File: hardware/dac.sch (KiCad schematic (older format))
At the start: 1 part

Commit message: Update schematics
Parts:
- added J?: JACK_V_OCT, symbol thonkiconn_jackSocket_fuzzySi:fuzzySI_thonkiconn
- added R?: 7.7k, symbol Device:R
- added R?: 10k, symbol Device:R
- added U? (x2): LM324, symbol Amplifier_Operational:LM324
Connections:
- net labels added: +12V
- wire segments 6 -> 18
- no-connect marks 1 -> 2
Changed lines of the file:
@@
 $EndComp
 Wire Wire Line
-	5600 3700 5600 4000
+	5600 3700 5600 3900
 $Comp
 L power:GND #PWR?
@@
 Wire Wire Line
 	4550 3400 5100 3400
+$Comp
+L Amplifier_Operational:LM324 U?
+U 1 1 5ED45991
+P 7850 3200
+F 0 "U?" H 7850 3567 50  0000 C CNN
+F 1 "LM324" H 7850 3476 50  0000 C CNN
+F 2 "" H 7800 3300 50  0001 C CNN
+F 3 "http://www.ti.com/lit/ds/symlink/lm2902-n.pdf" H 7900 3400 50  0001 C CNN
+	1    7850 3200
+	1    0    0    -1
+$EndComp
+$Comp
+L Amplifier_Operational:LM324 U?
+U 5 1 5ED45997
+P 7850 3200
+F 0 "U?" H 7808 3246 50  0000 L CNN
+F 1 "LM324" H 7808 3155 50  0000 L CNN
+F 2 "" H 7800 3300 50  0001 C CNN
+F 3 "http://www.ti.com/lit/ds/symlink/lm2902-n.pdf" H 7900 3400 50  0001 C CNN
+	5    7850 3200
+	1    0    0    -1
+$EndComp
+$Comp
+L Device:R R?
+U 1 1 5ED459B1
+P 7900 3900
+F 0 "R?" V 7693 3900 50  0000 C CNN
+F 1 "7.7k" V 7784 3900 50  0000 C CNN
+F 2 "" V 7830 3900 50  0001 C CNN
+F 3 "~" H 7900 3900 50  0001 C CNN
+	1    7900 3900
+	0    -1   -1   0
+$EndComp
+$Comp
+L power:GND #PWR?
+U 1 1 5ED459B7
+P 7750 3500
+F 0 "#PWR?" H 7750 3250 50  0001 C CNN
+F 1 "GND" H 7755 3327 50  0000 C CNN
+F 2 "" H 7750 3500 50  0001 C CNN
+F 3 "" H 7750 3500 50  0001 C CNN
+	1    7750 3500
+	1    0    0    -1
+$EndComp
+Wire Wire Line
+	8150 3200 8400 3200
+Wire Wire Line
+	7550 3300 7550 3900
+Wire Wire Line
+	7550 3900 7750 3900
+Wire Wire Line
+	8400 3200 8400 3900
+Wire Wire Line
+	8400 3900 8050 3900
+$Comp
+L power:+12V #PWR?
+U 1 1 5ED459C4
+P 7750 2700
+F 0 "#PWR?" H 7750 2550 50  0001 C CNN
+F 1 "+12V" H 7765 2873 50  0000 C CNN
+F 2 "" H 7750 2700 50  0001 C CNN
+F 3 "" H 7750 2700 50  0001 C CNN
+	1    7750 2700
+	1    0    0    -1
+$EndComp
+Wire Wire Line
+	7750 2700 7750 2900
+$Comp
+L Device:R R?
+U 1 1 5ED459CB
+P 6950 3900
+F 0 "R?" V 6743 3900 50  0000 C CNN
+F 1 "10k" V 6834 3900 50  0000 C CNN
+F 2 "" V 6880 3900 50  0001 C CNN
+F 3 "~" H 6950 3900 50  0001 C CNN
+	1    6950 3900
+	0    -1   -1   0
+$EndComp
+Wire Wire Line
+	7100 3900 7550 3900
+Connection ~ 7550 3900
+Wire Wire Line
+	5600 3900 6800 3900
+Connection ~ 5600 3900
+Wire Wire Line
+	5600 3900 5600 4000
+Wire Wire Line
+	6100 3100 7550 3100
+Wire Wire Line
+	8400 3200 9150 3200
+Connection ~ 8400 3200
+$Comp
+L power:GND #PWR?
+U 1 1 5ED51041
+P 9550 2850
+AR Path="/5ED37B53/5ED51041" Ref="#PWR?"  Part="1"
+AR Path="/5ED51041" Ref="#PWR?"  Part="1"
+F 0 "#PWR?" H 9550 2600 50  0001 C CNN
+F 1 "GND" H 9555 2677 50  0000 C CNN
+F 2 "" H 9550 2850 50  0001 C CNN
+F 3 "" H 9550 2850 50  0001 C CNN
+	1    9550 2850
+	-1   0    0    1
+$EndComp
+Wire Wire Line
+	9550 3000 9550 2850
+NoConn ~ 9150 3100
+$Comp
+L thonkiconn_jackSocket_fuzzySi:fuzzySI_thonkiconn J?
+U 1 1 5ED5104A
+P 9350 3100
+AR Path="/5ED37B53/5ED5104A" Ref="J?"  Part="1"
+AR Path="/5ED5104A" Ref="J?"  Part="1"
+F 0 "J?" H 9062 3076 50  0000 R CNN
+F 1 "JACK_V_OCT" H 9062 3167 50  0000 R CNN
+F 2 "" H 9600 3200 50  0001 C CNN
+F 3 "" H 9600 3200 50  0001 C CNN
+	1    9350 3100
+	-1   0    0    1
+$EndComp
 $EndSCHEMATC

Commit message: Add CV-out schematics
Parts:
- removed J?: JACK_V_OCT, symbol thonkiconn_jackSocket_fuzzySi:fuzzySI_thonkiconn
- removed R?: 7.7k, symbol Device:R
- removed R?: 10k, symbol Device:R
- removed U?: MCP4822, symbol Analog_DAC:MCP4822
- removed U? (x2): LM324, symbol Amplifier_Operational:LM324
- added C?: 220n, symbol Device:C
- added C?: 1u, symbol Device:C
- added C?: 100n, symbol Device:C
- added IC?: DAC8562SDGSR, SOP50P490X110-10N, symbol DAC8562:DAC8562SDGSR
- added R?: 10k, symbol Device:R
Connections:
- net labels added: 3v3_a, dac_avdd, dac_cs, dac_mosi, dac_sck, dac_vref
- net labels removed: +12V, +5V, CS, MOSI, SCK
- wire segments 18 -> 17
- no-connect marks 2 -> 0

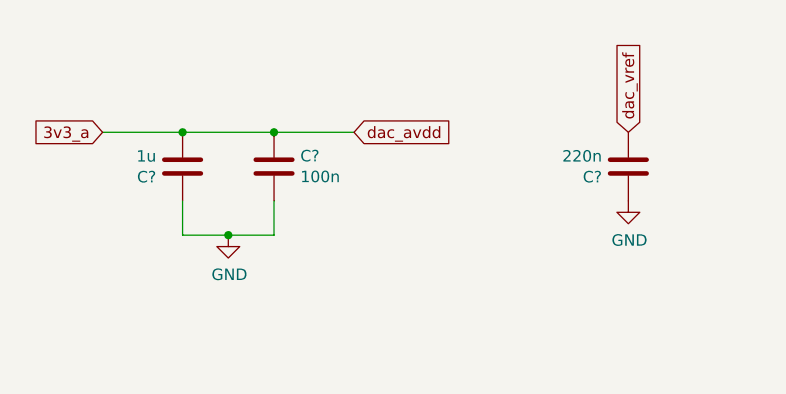
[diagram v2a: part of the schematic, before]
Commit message: Add CV inputs schematics
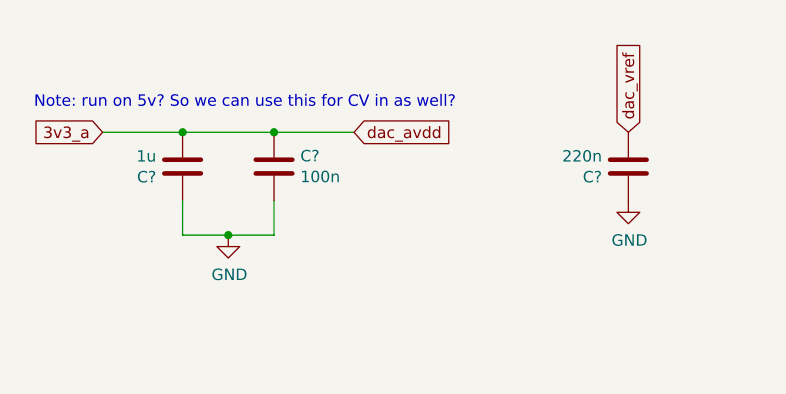
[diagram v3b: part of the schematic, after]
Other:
- note added: "Note: run on 5v? So we can use this for CV in as well?\n"
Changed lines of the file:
@@
 $Descr A4 11693 8268
 encoding utf-8
-Sheet 3 4
+Sheet 3 6
 Title ""
 Date ""
@@
 $EndDescr
 $Comp
-L power:GND #PWR011
+L power:GND #PWR?
 U 1 1 5ED3A9D0
 P 6400 3950
-F 0 "#PWR011" H 6400 3700 50  0001 C CNN
+F 0 "#PWR?" H 6400 3700 50  0001 C CNN
 F 1 "GND" V 6405 3822 50  0000 R CNN
 F 2 "" H 6400 3950 50  0001 C CNN
@@
 	1    0    0    -1
 $EndComp
-Connection ~ 5000 1850
-Wire Wire Line
-	5000 1850 4600 1850
-Wire Wire Line
-	5000 1850 5350 1850
 Wire Wire Line
 	4600 2150 4600 2300
@@
 Text GLabel 6550 1850 1    50   Input ~ 0
 dac_vref
+Wire Wire Line
+	4600 1850 5000 1850
+Connection ~ 5000 1850
+Wire Wire Line
+	5000 1850 5350 1850
+Text Notes 3950 1750 0    50   ~ 0
+Note: run on 5v? So we can use this for CV in as well?\n
 $EndSCHEMATC

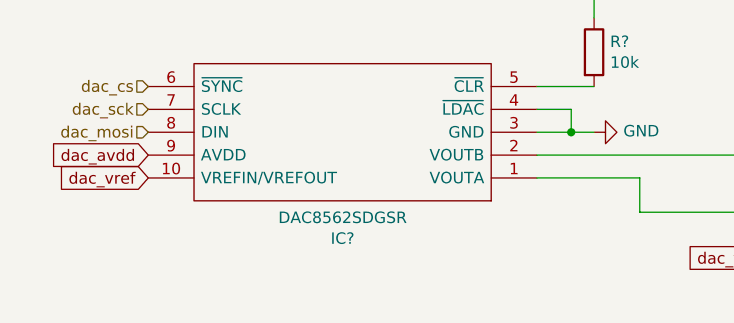
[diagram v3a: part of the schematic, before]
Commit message: Use DAC8564
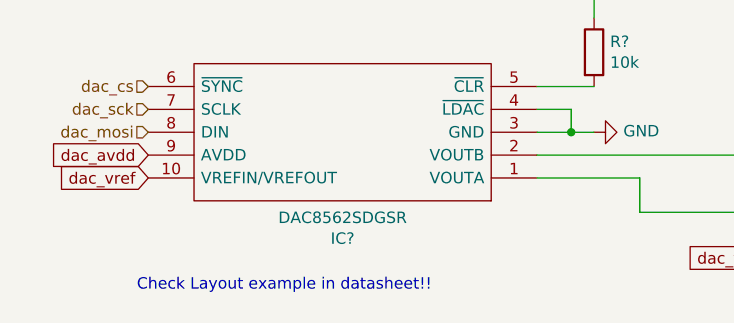
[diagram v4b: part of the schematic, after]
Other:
- note added: "Check Layout example in datasheet!!"
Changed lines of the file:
@@
 Text Notes 3950 1750 0    50   ~ 0
 Note: run on 5v? So we can use this for CV in as well?\n
+Text Notes 4400 4650 0    50   ~ 0
+Check Layout example in datasheet!!
 $EndSCHEMATC

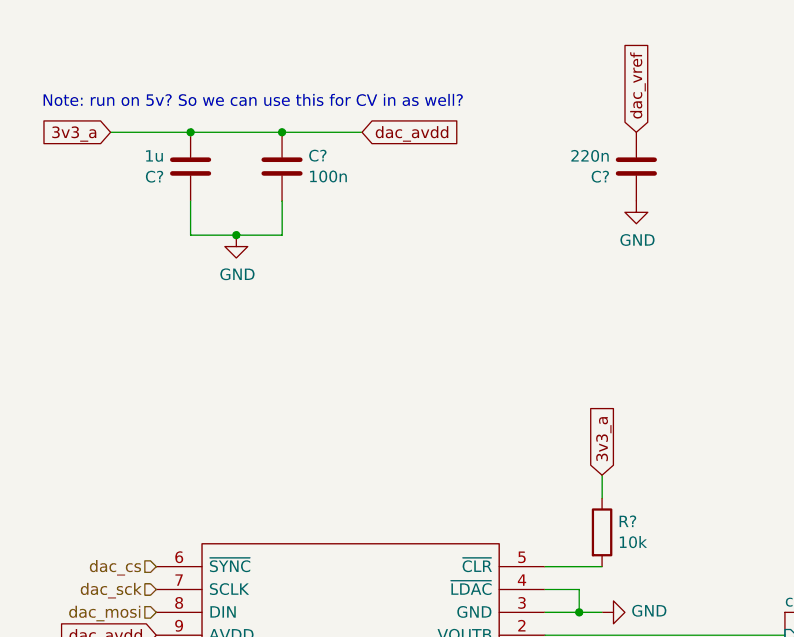
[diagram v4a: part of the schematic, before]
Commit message: Adjust CV-ins
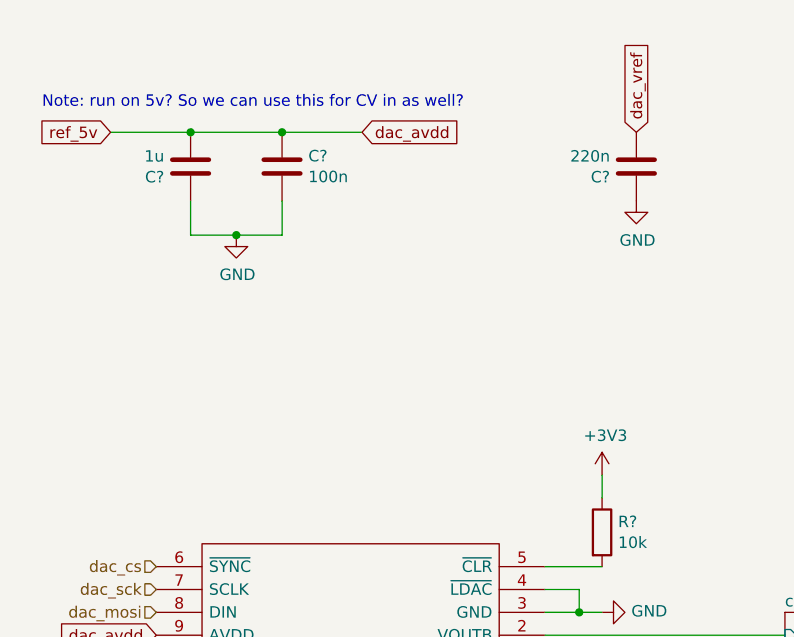
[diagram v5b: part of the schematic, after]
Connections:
- net 3v3_a renamed dac_avdd
- net dac_avdd: no longer R?.1
- new net +3V3: R?.1
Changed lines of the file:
@@
 Wire Wire Line
 	6300 3950 6400 3950
-Text GLabel 4250 1850 0    50   Input ~ 0
-3v3_a
 $Comp
 L Device:C C?
@@
 	1    0    0    -1
 $EndComp
-Connection ~ 4600 1850
 Wire Wire Line
 	4600 1850 4250 1850
@@
 Wire Wire Line
 	6150 3750 6400 3750
-Text GLabel 6400 3350 1    50   Input ~ 0
-3v3_a
 Wire Wire Line
 	6400 3450 6400 3350
@@
 dac_vref
 Wire Wire Line
-	4600 1850 5000 1850
-Connection ~ 5000 1850
-Wire Wire Line
 	5000 1850 5350 1850
 Text Notes 3950 1750 0    50   ~ 0
@@
 Text Notes 4400 4650 0    50   ~ 0
 Check Layout example in datasheet!!
+$Comp
+L power:+3V3 #PWR?
+U 1 1 5FD27C48
+P 6400 3350
+F 0 "#PWR?" H 6400 3200 50  0001 C CNN
+F 1 "+3V3" H 6415 3523 50  0000 C CNN
+F 2 "" H 6400 3350 50  0001 C CNN
+F 3 "" H 6400 3350 50  0001 C CNN
+	1    6400 3350
+	1    0    0    -1
+$EndComp
+Text GLabel 4250 1850 0    50   Input ~ 0
+ref_5v
+Wire Wire Line
+	4600 1850 5000 1850
+Connection ~ 4600 1850
+Connection ~ 5000 1850
 $EndSCHEMATC

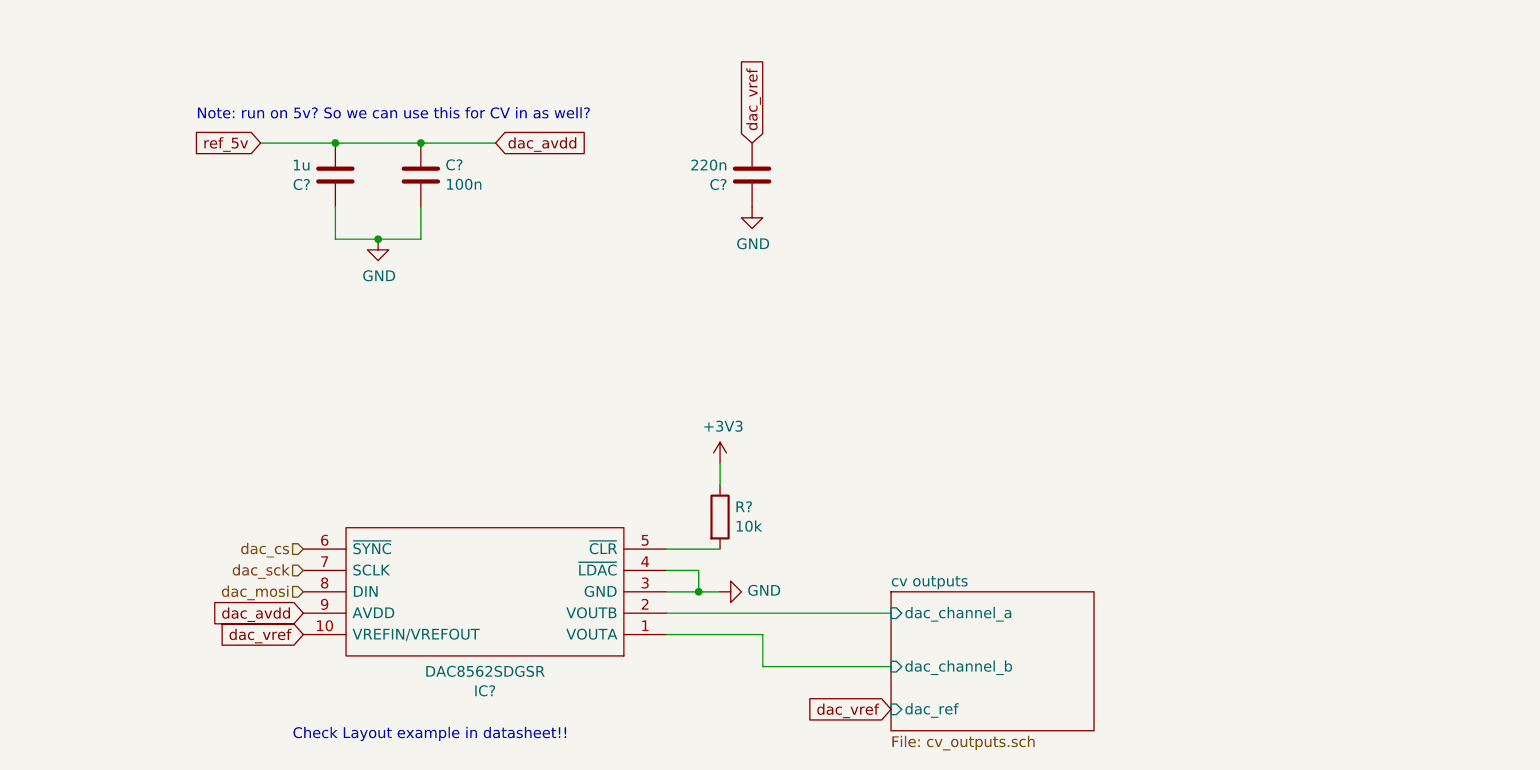
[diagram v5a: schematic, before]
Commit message: Add more schematics:
- Faders
- Step LEDs
- Trigger output
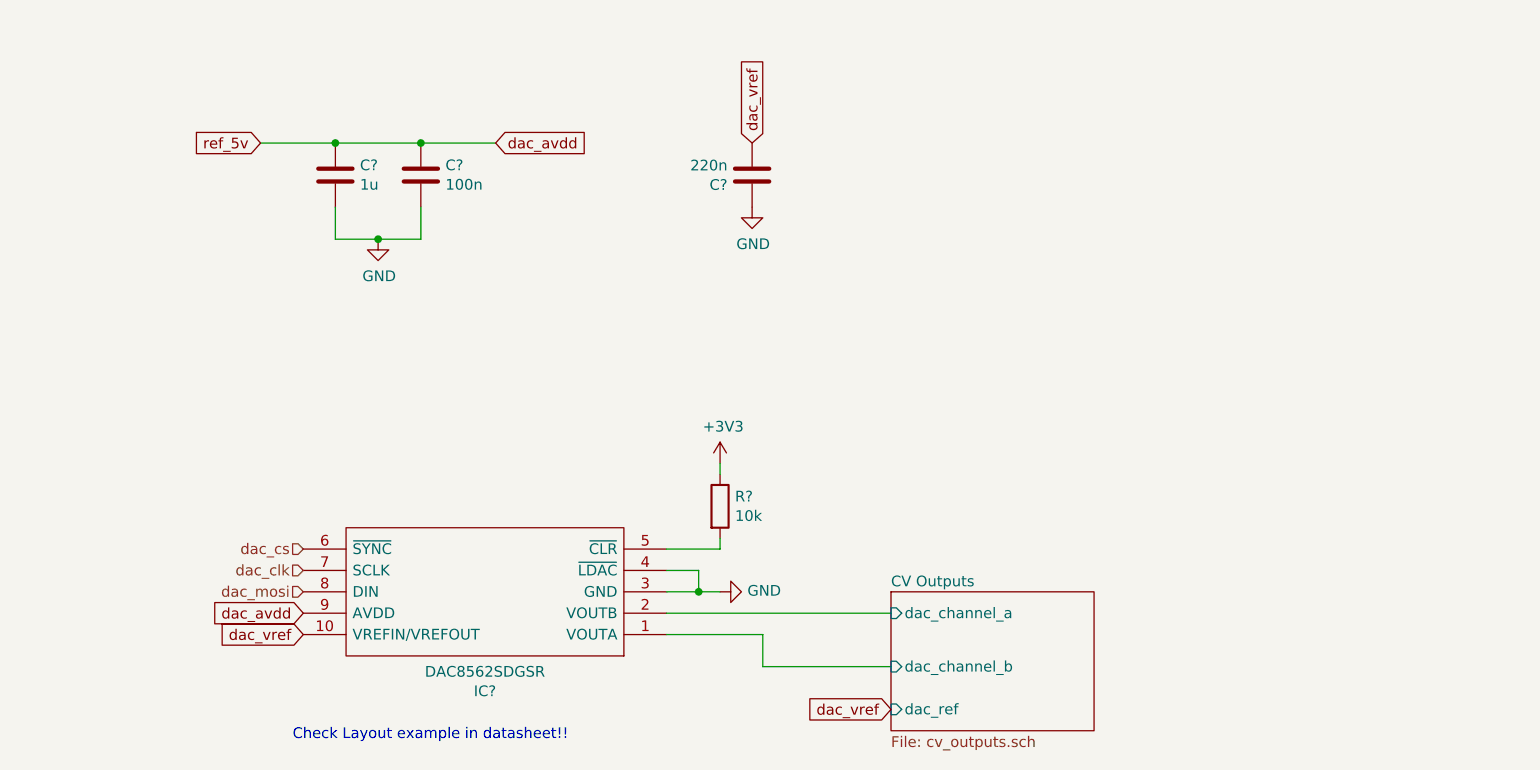
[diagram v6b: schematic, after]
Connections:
- net GND: now also C?.1; no longer C?.2
- net dac_avdd: now also C?.2; no longer C?.1
- net cv outputs/dac_channel_a renamed CV Outputs/dac_channel_a
- net cv outputs/dac_channel_b renamed CV Outputs/dac_channel_b
- net dac_sck renamed dac_clk
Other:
- note removed: "Note: run on 5v? So we can use this for CV in as well?\n"
- moved on the sheet: R?
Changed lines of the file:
@@
 $Descr A4 11693 8268
 encoding utf-8
-Sheet 3 6
+Sheet 3 9
 Title ""
 Date ""
@@
 $EndDescr
 $Comp
-L power:GND #PWR?
+L power:GND #PWR0106
 U 1 1 5ED3A9D0
 P 6400 3950
-F 0 "#PWR?" H 6400 3700 50  0001 C CNN
+F 0 "#PWR0106" H 6400 3700 50  0001 C CNN
 F 1 "GND" V 6405 3822 50  0000 R CNN
 F 2 "" H 6400 3950 50  0001 C CNN
@@
 $EndComp
 Text HLabel 4450 3850 0    50   Input ~ 0
-dac_sck
+dac_clk
 Text HLabel 4450 3950 0    50   Input ~ 0
 dac_mosi
@@
 $EndComp
 $Comp
-L power:GND #PWR?
+L power:GND #PWR0107
 U 1 1 5FB5E7F1
 P 6550 2150
-F 0 "#PWR?" H 6550 1900 50  0001 C CNN
+F 0 "#PWR0107" H 6550 1900 50  0001 C CNN
 F 1 "GND" H 6555 1977 50  0000 C CNN
 F 2 "" H 6550 2150 50  0001 C CNN
@@
 F 3 "~" H 4600 2000 50  0001 C CNN
 	1    4600 2000
-	1    0    0    -1
+	-1   0    0    1
 $EndComp
-Wire Wire Line
-	4600 1850 4250 1850
 $Comp
-L power:GND #PWR?
+L power:GND #PWR0108
 U 1 1 5FB62572
 P 4800 2300
-F 0 "#PWR?" H 4800 2050 50  0001 C CNN
+F 0 "#PWR0108" H 4800 2050 50  0001 C CNN
 F 1 "GND" H 4805 2127 50  0000 C CNN
 F 2 "" H 4800 2300 50  0001 C CNN
@@
 Wire Wire Line
 	6600 4300 7200 4300
-$Comp
-L Device:R R?
-U 1 1 5FB72111
-P 6400 3600
-F 0 "R?" H 6470 3646 50  0000 L CNN
-F 1 "10k" H 6470 3555 50  0000 L CNN
-F 2 "" V 6330 3600 50  0001 C CNN
-F 3 "~" H 6400 3600 50  0001 C CNN
-	1    6400 3600
-	1    0    0    -1
-$EndComp
-Wire Wire Line
-	6150 3750 6400 3750
-Wire Wire Line
-	6400 3450 6400 3350
 $Sheet
 S 7200 3950 950  650
 U 5FB5AC07
-F0 "cv outputs" 50
+F0 "CV Outputs" 50
 F1 "cv_outputs.sch" 50
 F2 "dac_channel_a" I L 7200 4050 50
@@
 Wire Wire Line
 	5000 1850 5350 1850
-Text Notes 3950 1750 0    50   ~ 0
-Note: run on 5v? So we can use this for CV in as well?\n
 Text Notes 4400 4650 0    50   ~ 0
 Check Layout example in datasheet!!
 $Comp
-L power:+3V3 #PWR?
+L power:+3V3 #PWR0109
 U 1 1 5FD27C48
 P 6400 3350
-F 0 "#PWR?" H 6400 3200 50  0001 C CNN
+F 0 "#PWR0109" H 6400 3200 50  0001 C CNN
 F 1 "+3V3" H 6415 3523 50  0000 C CNN
 F 2 "" H 6400 3350 50  0001 C CNN
@@
 Text GLabel 4250 1850 0    50   Input ~ 0
 ref_5v
+Connection ~ 5000 1850
+Wire Wire Line
+	4250 1850 4600 1850
+Connection ~ 4600 1850
 Wire Wire Line
 	4600 1850 5000 1850
-Connection ~ 4600 1850
-Connection ~ 5000 1850
+Wire Wire Line
+	6150 3750 6400 3750
+Wire Wire Line
+	6400 3750 6400 3700
+$Comp
+L Device:R R?
+U 1 1 5FB72111
+P 6400 3550
+F 0 "R?" H 6470 3596 50  0000 L CNN
+F 1 "10k" H 6470 3505 50  0000 L CNN
+F 2 "" V 6330 3550 50  0001 C CNN
+F 3 "~" H 6400 3550 50  0001 C CNN
+	1    6400 3550
+	1    0    0    -1
+$EndComp
+Wire Wire Line
+	6400 3350 6400 3400
 $EndSCHEMATC
